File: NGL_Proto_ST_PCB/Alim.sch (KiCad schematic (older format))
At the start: 14 parts, among them U5 LF33CDT-TR, U6 MAX860ESA+T

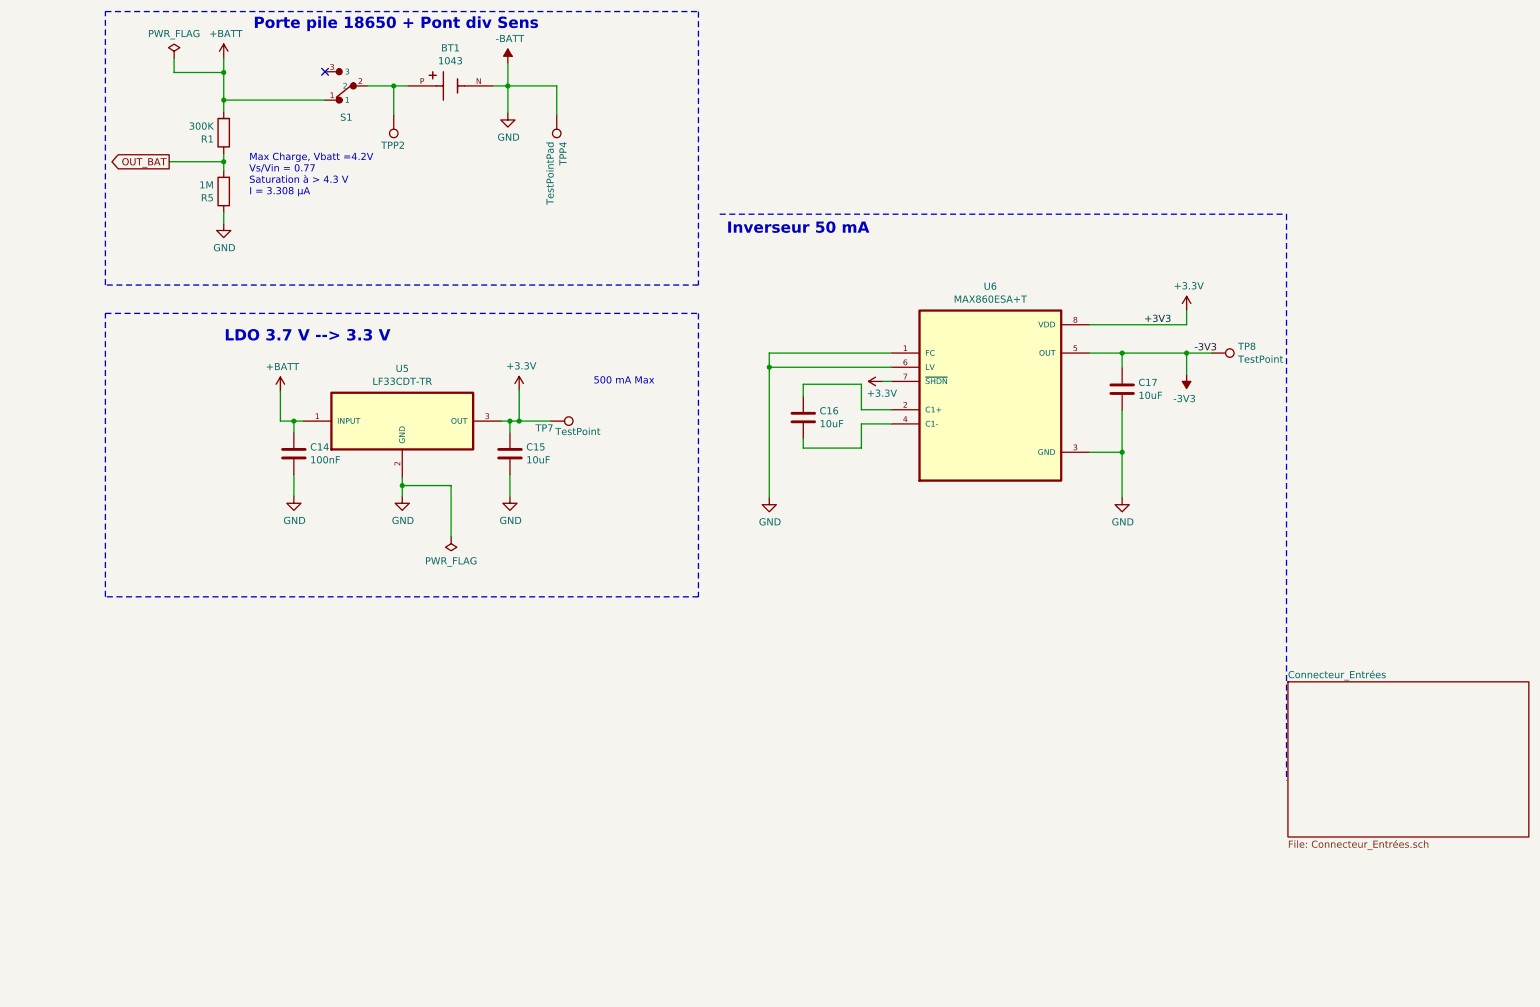
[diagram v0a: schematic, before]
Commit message: Rrecherche sur pot num et mise en page
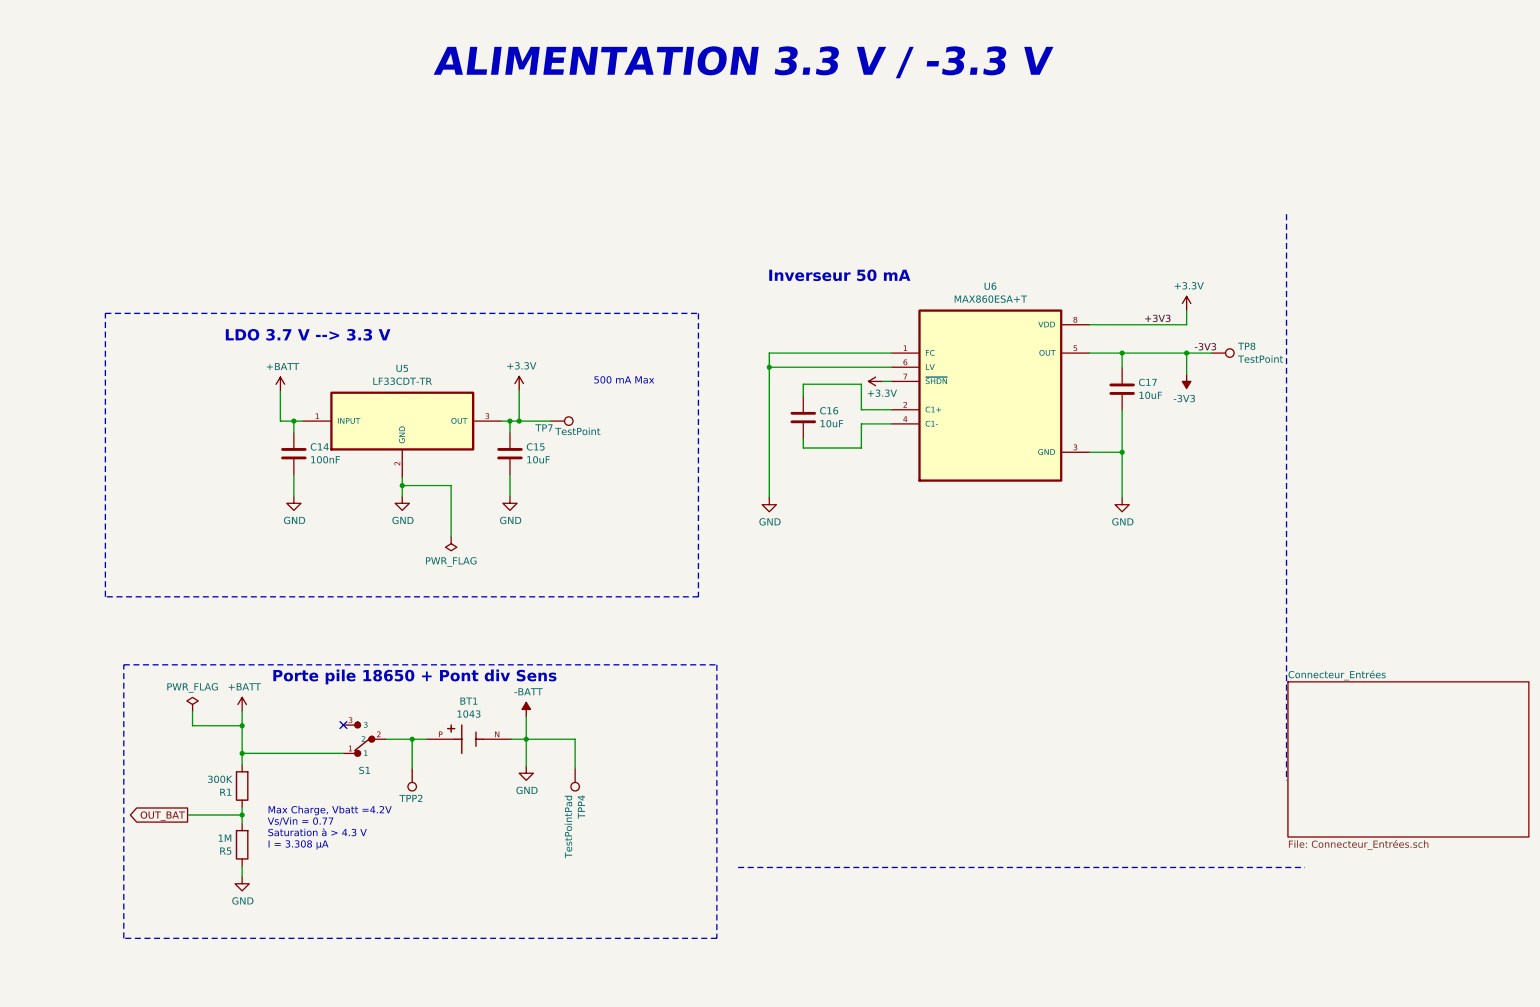
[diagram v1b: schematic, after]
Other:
- note added: "ALIMENTATION 3.3 V / -3.3 V"
- moved on the sheet: BT1, R1, R5, S1, TPP2, TPP4
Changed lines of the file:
@@
 $Descr A4 11693 8268
 encoding utf-8
-Sheet 3 5
-Title "NGL_Proto"
-Date "2022-05-02"
-Rev "V1"
+Sheet 3 6
+Title "NGL_Proto_V2"
+Date "2022-05-27"
+Rev "V2"
 Comp "ADTP"
-Comment1 "Usinage by LPKF"
-Comment2 ""
-Comment3 ""
+Comment1 "Auteur: Benoît"
+Comment2 "Proto avec potar numérique + intégration"
+Comment3 "Sous traité chez JLCPCB"
 Comment4 ""
 $EndDescr
@@
 L 1043:1043 BT1
 U 1 1 628EF407
-P 3600 1095
-F 0 "BT1" H 3600 1362 50  0000 C CNN
-F 1 "1043" H 3600 1271 50  0000 C CNN
-F 2 "Lib_NGL_Proto:BAT_1043" H 3600 1095 50  0001 L BNN
-F 3 "https://www.mouser.fr/datasheet/2/215/1043-745411.pdf" H 3600 1095 50  0001 L BNN
-F 4 "Keystone" H 3600 1095 50  0001 L BNN "MANUFACTURER"
-F 5 "1043" H 3600 1095 50  0001 C CNN "MPN"
-	1    3600 1095
+P 3730 5705
+F 0 "BT1" H 3730 5972 50  0000 C CNN
+F 1 "1043" H 3730 5881 50  0000 C CNN
+F 2 "Lib_NGL_Proto:BAT_1043" H 3730 5705 50  0001 L BNN
+F 3 "https://www.mouser.fr/datasheet/2/215/1043-745411.pdf" H 3730 5705 50  0001 L BNN
+F 4 "Keystone" H 3730 5705 50  0001 L BNN "MANUFACTURER"
+F 5 "1043" H 3730 5705 50  0001 C CNN "MPN"
+	1    3730 5705
 	1    0    0    -1
 $EndComp
@@
 L Connector:TestPoint TPP2
 U 1 1 62710BD9
-P 3200 1300
-F 0 "TPP2" H 3205 1515 50  0000 C CNN
-F 1 "TestPointPad" V 3304 1372 50  0001 C CNN
-F 2 "TestPoint:TestPoint_Pad_D3.0mm" H 3400 1300 50  0001 C CNN
-F 3 "~" H 3400 1300 50  0001 C CNN
-	1    3200 1300
+P 3330 5910
+F 0 "TPP2" H 3335 6125 50  0000 C CNN
+F 1 "TestPointPad" V 3434 5982 50  0001 C CNN
+F 2 "TestPoint:TestPoint_Pad_D3.0mm" H 3530 5910 50  0001 C CNN
+F 3 "~" H 3530 5910 50  0001 C CNN
+	1    3330 5910
 	-1   0    0    1
 $EndComp
@@
 L Connector:TestPoint TPP4
 U 1 1 627111ED
-P 4350 1300
-F 0 "TPP4" V 4304 1488 50  0000 L CNN
-F 1 "TestPointPad" V 4395 1488 50  0000 L CNN
-F 2 "TestPoint:TestPoint_Pad_4.0x4.0mm" H 4550 1300 50  0001 C CNN
-F 3 "~" H 4550 1300 50  0001 C CNN
-	1    4350 1300
+P 4480 5910
+F 0 "TPP4" V 4434 6098 50  0000 L CNN
+F 1 "TestPointPad" V 4525 6098 50  0000 L CNN
+F 2 "TestPoint:TestPoint_Pad_4.0x4.0mm" H 4680 5910 50  0001 C CNN
+F 3 "~" H 4680 5910 50  0001 C CNN
+	1    4480 5910
 	-1   0    0    1
 $EndComp
@@
 L power:+BATT #PWR017
 U 1 1 62711824
-P 2000 900
-F 0 "#PWR017" H 2000 750 50  0001 C CNN
-F 1 "+BATT" H 2015 1073 50  0000 C CNN
-F 2 "" H 2000 900 50  0001 C CNN
-F 3 "" H 2000 900 50  0001 C CNN
-	1    2000 900
+P 2130 5510
+F 0 "#PWR017" H 2130 5360 50  0001 C CNN
+F 1 "+BATT" H 2145 5683 50  0000 C CNN
+F 2 "" H 2130 5510 50  0001 C CNN
+F 3 "" H 2130 5510 50  0001 C CNN
+	1    2130 5510
 	1    0    0    -1
 $EndComp
@@
 L power:-BATT #PWR019
 U 1 1 62711F03
-P 4005 935
-F 0 "#PWR019" H 4005 785 50  0001 C CNN
-F 1 "-BATT" H 4020 1108 50  0000 C CNN
-F 2 "" H 4005 935 50  0001 C CNN
-F 3 "" H 4005 935 50  0001 C CNN
-	1    4005 935
+P 4135 5545
+F 0 "#PWR019" H 4135 5395 50  0001 C CNN
+F 1 "-BATT" H 4150 5718 50  0000 C CNN
+F 2 "" H 4135 5545 50  0001 C CNN
+F 3 "" H 4135 5545 50  0001 C CNN
+	1    4135 5545
 	1    0    0    -1
 $EndComp
@@
 Text Notes 2005 2910 0    79   ~ 16
 LDO 3.7 V --> 3.3 V
-Text Notes 2210 705  0    79   ~ 16
+Text Notes 2340 5315 0    79   ~ 16
 Porte pile 18650 + Pont div Sens
 Wire Notes Line
-	5500 2000 9500 2000
+	5630 6610 9630 6610
 Wire Notes Line
 	9500 2000 9500 6000
-Text Notes 5550 2150 0    79   ~ 16
+Text Notes 5840 2490 0    79   ~ 16
 Inverseur 50 mA
 Wire Wire Line
@@
 L power:PWR_FLAG #FLG0101
 U 1 1 627F6B65
-P 1650 900
-F 0 "#FLG0101" H 1650 975 50  0001 C CNN
-F 1 "PWR_FLAG" H 1650 1073 50  0000 C CNN
-F 2 "" H 1650 900 50  0001 C CNN
-F 3 "~" H 1650 900 50  0001 C CNN
-	1    1650 900
+P 1780 5510
+F 0 "#FLG0101" H 1780 5585 50  0001 C CNN
+F 1 "PWR_FLAG" H 1780 5683 50  0000 C CNN
+F 2 "" H 1780 5510 50  0001 C CNN
+F 3 "~" H 1780 5510 50  0001 C CNN
+	1    1780 5510
 	1    0    0    -1
 $EndComp
@@
 L Device:R R?
 U 1 1 628AB478
-P 2000 1425
+P 2130 6035
 AR Path="/6271F3E2/62744FDF/6271D84F/628AB478" Ref="R?"  Part="1"
 AR Path="/6271F3E2/62744FDF/628AB478" Ref="R1"  Part="1"
-F 0 "R1" H 2070 1471 50  0000 L CNN
-F 1 "300K" H 2070 1380 50  0000 L CNN
-F 2 "Resistor_SMD:R_0805_2012Metric" V 1930 1425 50  0001 C CNN
-F 3 "~" H 2000 1425 50  0001 C CNN
-	1    2000 1425
+F 0 "R1" H 2200 6081 50  0000 L CNN
+F 1 "300K" H 2200 5990 50  0000 L CNN
+F 2 "Resistor_SMD:R_0805_2012Metric" V 2060 6035 50  0001 C CNN
+F 3 "~" H 2130 6035 50  0001 C CNN
+	1    2130 6035
 	-1   0    0    1
 $EndComp
@@
 L Device:R R?
 U 1 1 628AC10E
-P 2000 1840
+P 2130 6450
 AR Path="/6271F3E2/62744FDF/6271D84F/628AC10E" Ref="R?"  Part="1"
 AR Path="/6271F3E2/62744FDF/628AC10E" Ref="R5"  Part="1"
-F 0 "R5" H 2070 1886 50  0000 L CNN
-F 1 "1M" H 2070 1795 50  0000 L CNN
-F 2 "Resistor_SMD:R_0805_2012Metric" V 1930 1840 50  0001 C CNN
-F 3 "~" H 2000 1840 50  0001 C CNN
-	1    2000 1840
+F 0 "R5" H 2200 6496 50  0000 L CNN
+F 1 "1M" H 2200 6405 50  0000 L CNN
+F 2 "Resistor_SMD:R_0805_2012Metric" V 2060 6450 50  0001 C CNN
+F 3 "~" H 2130 6450 50  0001 C CNN
+	1    2130 6450
 	-1   0    0    1
 $EndComp
@@
 L power:GND #PWR012
 U 1 1 628B160D
-P 2000 2065
-F 0 "#PWR012" H 2000 1815 50  0001 C CNN
-F 1 "GND" H 2005 1892 50  0000 C CNN
-F 2 "" H 2000 2065 50  0001 C CNN
-F 3 "" H 2000 2065 50  0001 C CNN
-	1    2000 2065
+P 2130 6675
+F 0 "#PWR012" H 2130 6425 50  0001 C CNN
+F 1 "GND" H 2135 6502 50  0000 C CNN
+F 2 "" H 2130 6675 50  0001 C CNN
+F 3 "" H 2130 6675 50  0001 C CNN
+	1    2130 6675
 	1    0    0    -1
 $EndComp
 Wire Wire Line
-	2000 1690 2000 1630
+	2130 6300 2130 6240
 Wire Wire Line
-	2000 2065 2000 1990
-Text GLabel 1615 1630 0    50   Output ~ 0
+	2130 6675 2130 6600
+Text GLabel 1745 6240 0    50   Output ~ 0
 OUT_BAT
 Wire Wire Line
-	1615 1630 2000 1630
-Connection ~ 2000 1630
+	1745 6240 2130 6240
+Connection ~ 2130 6240
 Wire Wire Line
-	2000 1630 2000 1575
-Text Notes 2180 1875 0    50   ~ 0
+	2130 6240 2130 6185
+Text Notes 2310 6485 0    50   ~ 0
 Max Charge, Vbatt =4.2V\nVs/Vin = 0.77\nSaturation à > 4.3 V\nI = 3.308 μA
 $Comp
@@
 L 1101M2S3CQE2:1101M2S3CQE2 S1
 U 1 1 62A4F233
-P 2915 1095
-F 0 "S1" H 2965 1317 50  0000 C CNN
-F 1 "1101M2S3CQE2" H 2965 1318 50  0001 C CNN
-F 2 "Lib_NGL_Proto:SW_1101M2S3CQE2" H 2915 1095 50  0001 L BNN
-F 3 "https://docs.rs-online.com/eaa8/0900766b800993da.pdf" H 2915 1095 50  0001 L BNN
-F 4 "CnK" H 2915 1095 50  0001 L BNN "MANUFACTURER"
-	1    2915 1095
+P 3045 5705
+F 0 "S1" H 3095 5927 50  0000 C CNN
+F 1 "1101M2S3CQE2" H 3095 5928 50  0001 C CNN
+F 2 "Lib_NGL_Proto:SW_1101M2S3CQE2" H 3045 5705 50  0001 L BNN
+F 3 "https://docs.rs-online.com/eaa8/0900766b800993da.pdf" H 3045 5705 50  0001 L BNN
+F 4 "CnK" H 3045 5705 50  0001 L BNN "MANUFACTURER"
+	1    3045 5705
 	-1   0    0    1
 $EndComp
@@
 L power:GND #PWR049
 U 1 1 62A5D6DC
-P 4005 1285
-F 0 "#PWR049" H 4005 1035 50  0001 C CNN
-F 1 "GND" H 4010 1112 50  0000 C CNN
-F 2 "" H 4005 1285 50  0001 C CNN
-F 3 "" H 4005 1285 50  0001 C CNN
-	1    4005 1285
+P 4135 5895
+F 0 "#PWR049" H 4135 5645 50  0001 C CNN
+F 1 "GND" H 4140 5722 50  0000 C CNN
+F 2 "" H 4135 5895 50  0001 C CNN
+F 3 "" H 4135 5895 50  0001 C CNN
+	1    4135 5895
 	1    0    0    -1
 $EndComp
 Wire Wire Line
-	4005 1285 4005 1095
-Connection ~ 4005 1095
+	4135 5895 4135 5705
+Connection ~ 4135 5705
 Wire Wire Line
-	4005 1095 3900 1095
+	4135 5705 4030 5705
 Wire Wire Line
-	4005 935  4005 1095
+	4135 5545 4135 5705
 Wire Wire Line
 	4020 3460 4020 3540
@@
 Connection ~ 4085 3460
 Wire Wire Line
-	3015 1095 3200 1095
+	3145 5705 3330 5705
 Wire Wire Line
-	2000 1275 2000 1195
+	2130 5885 2130 5805
 Wire Wire Line
-	2715 1195 2000 1195
-Connection ~ 2000 1195
+	2845 5805 2130 5805
+Connection ~ 2130 5805
 Wire Wire Line
-	2000 1195 2000 1000
+	2130 5805 2130 5610
 Wire Wire Line
-	1650 900  1650 1000
+	1780 5510 1780 5610
 Wire Wire Line
-	1650 1000 2000 1000
-Connection ~ 2000 1000
+	1780 5610 2130 5610
+Connection ~ 2130 5610
 Wire Wire Line
-	2000 1000 2000 900
+	2130 5610 2130 5510
 Wire Wire Line
-	3200 1300 3200 1095
-Connection ~ 3200 1095
+	3330 5910 3330 5705
+Connection ~ 3330 5705
 Wire Wire Line
-	3200 1095 3300 1095
+	3330 5705 3430 5705
 Wire Wire Line
-	4350 1095 4350 1300
+	4480 5705 4480 5910
 Wire Wire Line
-	4005 1095 4350 1095
+	4135 5705 4480 5705
 Wire Notes Line
-	5350 2500 1165 2500
+	5480 7110 1295 7110
 Wire Notes Line
-	1165 2500 1165 570
+	1295 7110 1295 5180
 Wire Notes Line
-	1165 570  5350 570
+	1295 5180 5480 5180
 Wire Notes Line
-	5350 570  5350 2500
+	5480 5180 5480 7110
 $Comp
 L power:+BATT #PWR0112
@@
 	2400 3460 2400 3250
 Connection ~ 2495 3460
-NoConn ~ 2715 995
+NoConn ~ 2845 5605
 Text Label 8495 2780 0    50   ~ 0
 +3V3
+Text Notes 3480 1050 0    197  Italic 39
+ALIMENTATION 3.3 V / -3.3 V
 $EndSCHEMATC

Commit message: amélioration
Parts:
- added M?: C0720B001F, Lib_NGL_ST:XDCR_C0720B001F, symbol C0720B001F:C0720B001F
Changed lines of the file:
@@
 U 1 1 62775941
 P 8970 2980
-F 0 "TP8" V 8924 3168 50  0000 L CNN
-F 1 "TestPoint" V 9015 3168 50  0000 L CNN
+F 0 "TP8" V 8845 3025 50  0000 L CNN
+F 1 "TestPoint" V 9050 2890 50  0000 L CNN
 F 2 "Connector_PinHeader_2.54mm:PinHeader_1x01_P2.54mm_Vertical" H 9170 2980 50  0001 C CNN
 F 3 "~" H 9170 2980 50  0001 C CNN
@@
 Text Notes 2340 5315 0    79   ~ 16
 Porte pile 18650 + Pont div Sens
-Wire Notes Line
-	5630 6610 9630 6610
-Wire Notes Line
-	9500 2000 9500 6000
-Text Notes 5840 2490 0    79   ~ 16
+Text Notes 5725 2210 0    79   ~ 16
 Inverseur 50 mA
 Wire Wire Line
@@
 Text Notes 3480 1050 0    197  Italic 39
 ALIMENTATION 3.3 V / -3.3 V
+Wire Notes Line
+	9255 2270 9255 6265
+Wire Notes Line
+	9255 6265 5675 6265
+Wire Notes Line
+	5675 6265 5675 2270
+Wire Notes Line
+	5675 2270 9255 2270
+$Comp
+L C0720B001F:C0720B001F M?
+U 1 1 629D5EFD
+P 2045 1885
+F 0 "M?" H 2273 1931 50  0000 L CNN
+F 1 "C0720B001F" H 2273 1840 50  0000 L CNN
+F 2 "Lib_NGL_ST:XDCR_C0720B001F" H 2045 1885 50  0001 L BNN
+F 3 "" H 2045 1885 50  0001 L BNN
+F 4 "Jinlong Machinery" H 2045 1885 50  0001 L BNN "MF"
+	1    2045 1885
+	1    0    0    -1
+$EndComp
+$Comp
+L power:+3.3V #PWR?
+U 1 1 629D6C67
+P 2350 1220
+F 0 "#PWR?" H 2350 1070 50  0001 C CNN
+F 1 "+3.3V" H 2365 1393 50  0000 C CNN
+F 2 "" H 2350 1220 50  0001 C CNN
+F 3 "" H 2350 1220 50  0001 C CNN
+	1    2350 1220
+	1    0    0    -1
+$EndComp
+$Comp
+L power:GND #PWR?
+U 1 1 629D766E
+P 1645 2385
+F 0 "#PWR?" H 1645 2135 50  0001 C CNN
+F 1 "GND" H 1650 2212 50  0000 C CNN
+F 2 "" H 1645 2385 50  0001 C CNN
+F 3 "" H 1645 2385 50  0001 C CNN
+	1    1645 2385
+	1    0    0    -1
+$EndComp
 $EndSCHEMATC
